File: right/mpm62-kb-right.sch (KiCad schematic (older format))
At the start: 86 parts

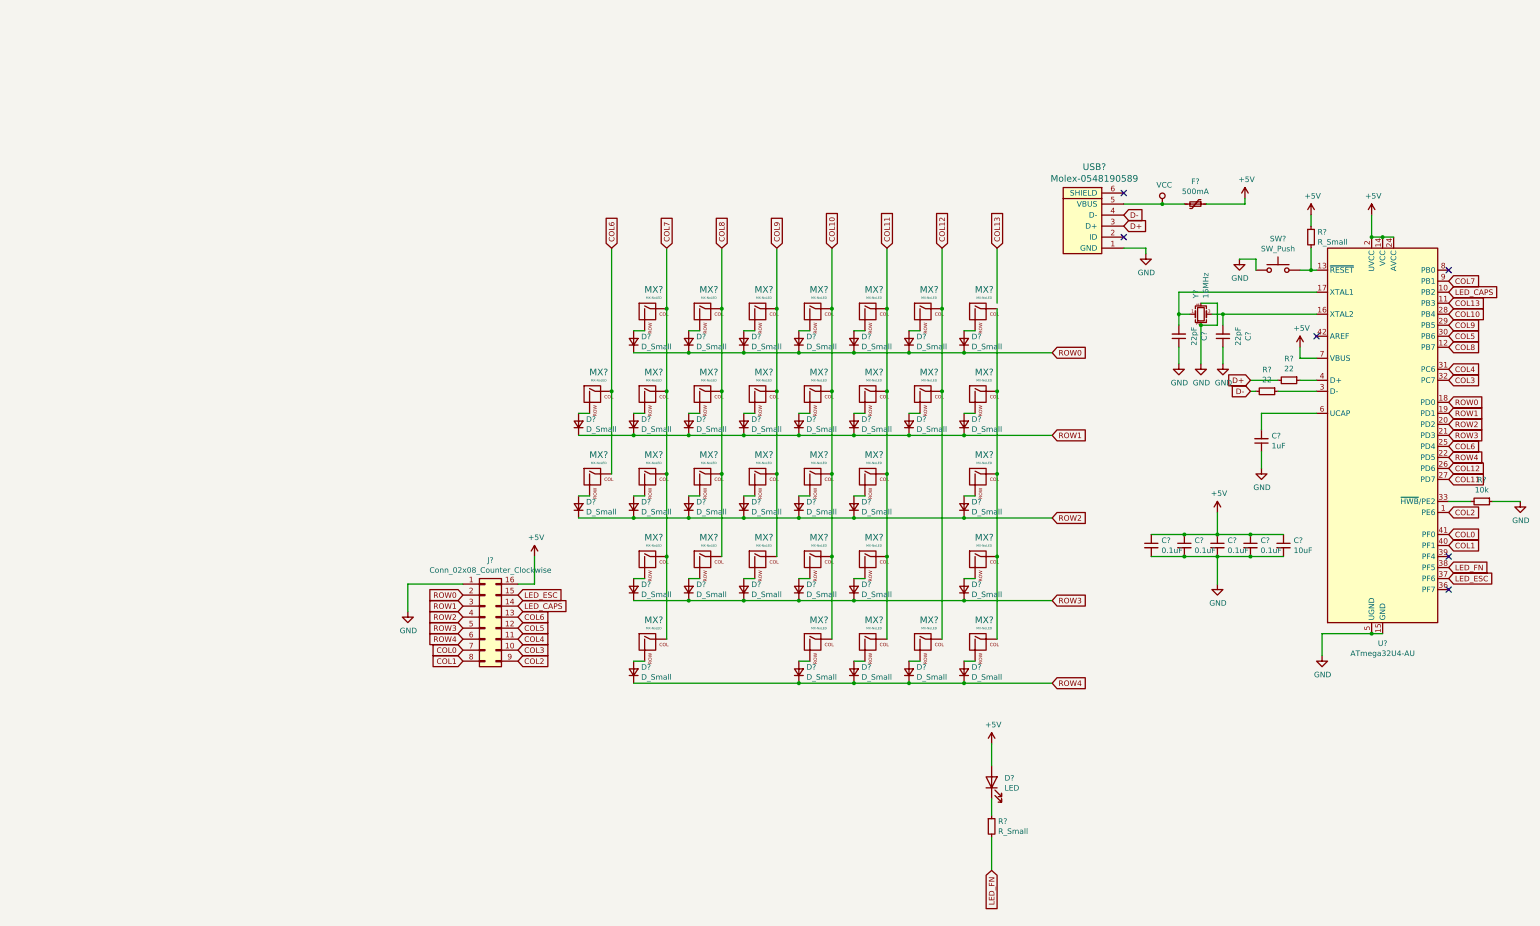
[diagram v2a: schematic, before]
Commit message: Annotated components
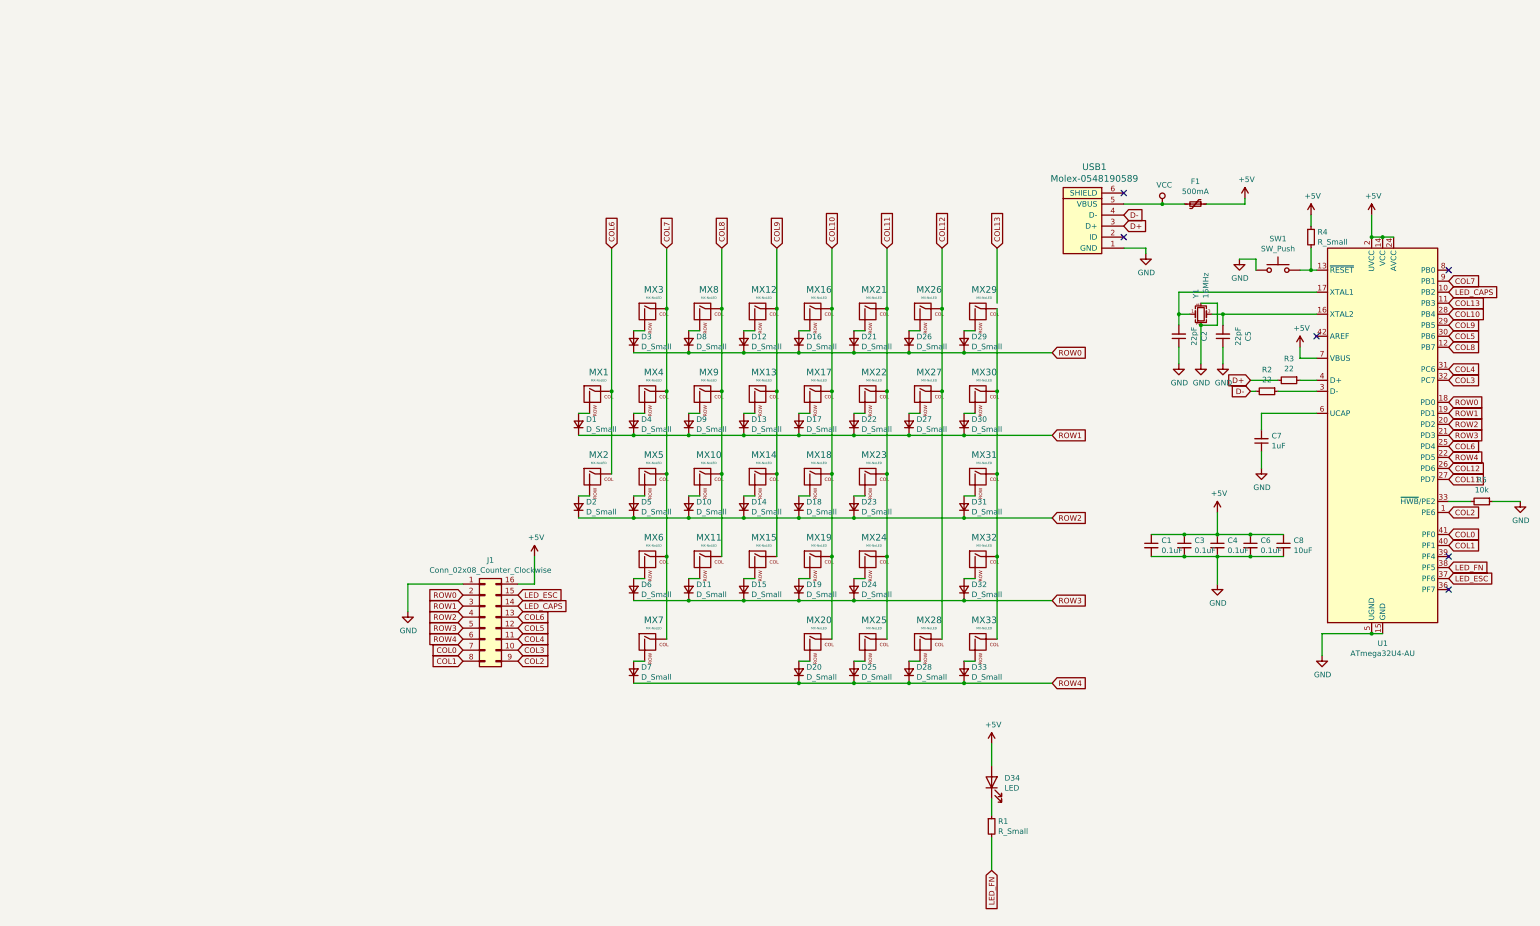
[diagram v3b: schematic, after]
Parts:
- gave numbers to parts that had none: 86

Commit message: Assigned footprints
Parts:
- C1, C2, C3, C4, C5, C6, C7, C8: footprint (none) -> Capacitor_SMD:C_0805_2012Metric
- D1, D10, D11, D12, D13, D14, D15, D16, D17, D18, D19, D2, D20, D21, D22, D23, D24, D25, D26, D27, D28, D29, D3, D30, D31, D32, D33, D4, D5, D6, D7, D8, D9: footprint (none) -> Diode_SMD:D_SOD-123
- D34: footprint (none) -> LED_SMD:LED_0805_2012Metric
- F1: footprint (none) -> Fuse:Fuse_1206_3216Metric
- J1: footprint (none) -> Connector_PinSocket_2.54mm:PinSocket_2x08_P2.54mm_Vertical
- MX1, MX10, MX11, MX12, MX13, MX14, MX15, MX16, MX17, MX18, MX19, MX2, MX21, MX22, MX23, MX24, MX26, MX27, MX3, MX4, MX5, MX6, MX8, MX9: footprint (none) -> MX_Alps_Hybrid:MX-1U-NoLED
- MX20, MX25, MX28, MX33: footprint (none) -> MX_Alps_Hybrid:MX-1.25U-NoLED
- MX29: footprint (none) -> MX_Alps_Hybrid:MX-2U-NoLED
- MX30: footprint (none) -> MX_Alps_Hybrid:MX-1.5U-NoLED
- MX31: footprint (none) -> MX_Alps_Hybrid:MX-2.25U-NoLED
- MX32: footprint (none) -> MX_Alps_Hybrid:MX-2.75U-NoLED
- MX7: footprint (none) -> MX_Alps_Hybrid:MX-3U-NoLED
- R1, R2, R3, R4, R5: footprint (none) -> Resistor_SMD:R_0805_2012Metric
- SW1: footprint (none) -> random-keyboard-parts:SKQG-1155865
- USB1: footprint (none) -> random-keyboard-parts:Molex-0548190589
- Y1: footprint (none) -> Crystal:Crystal_SMD_3225-4Pin_3.2x2.5mm

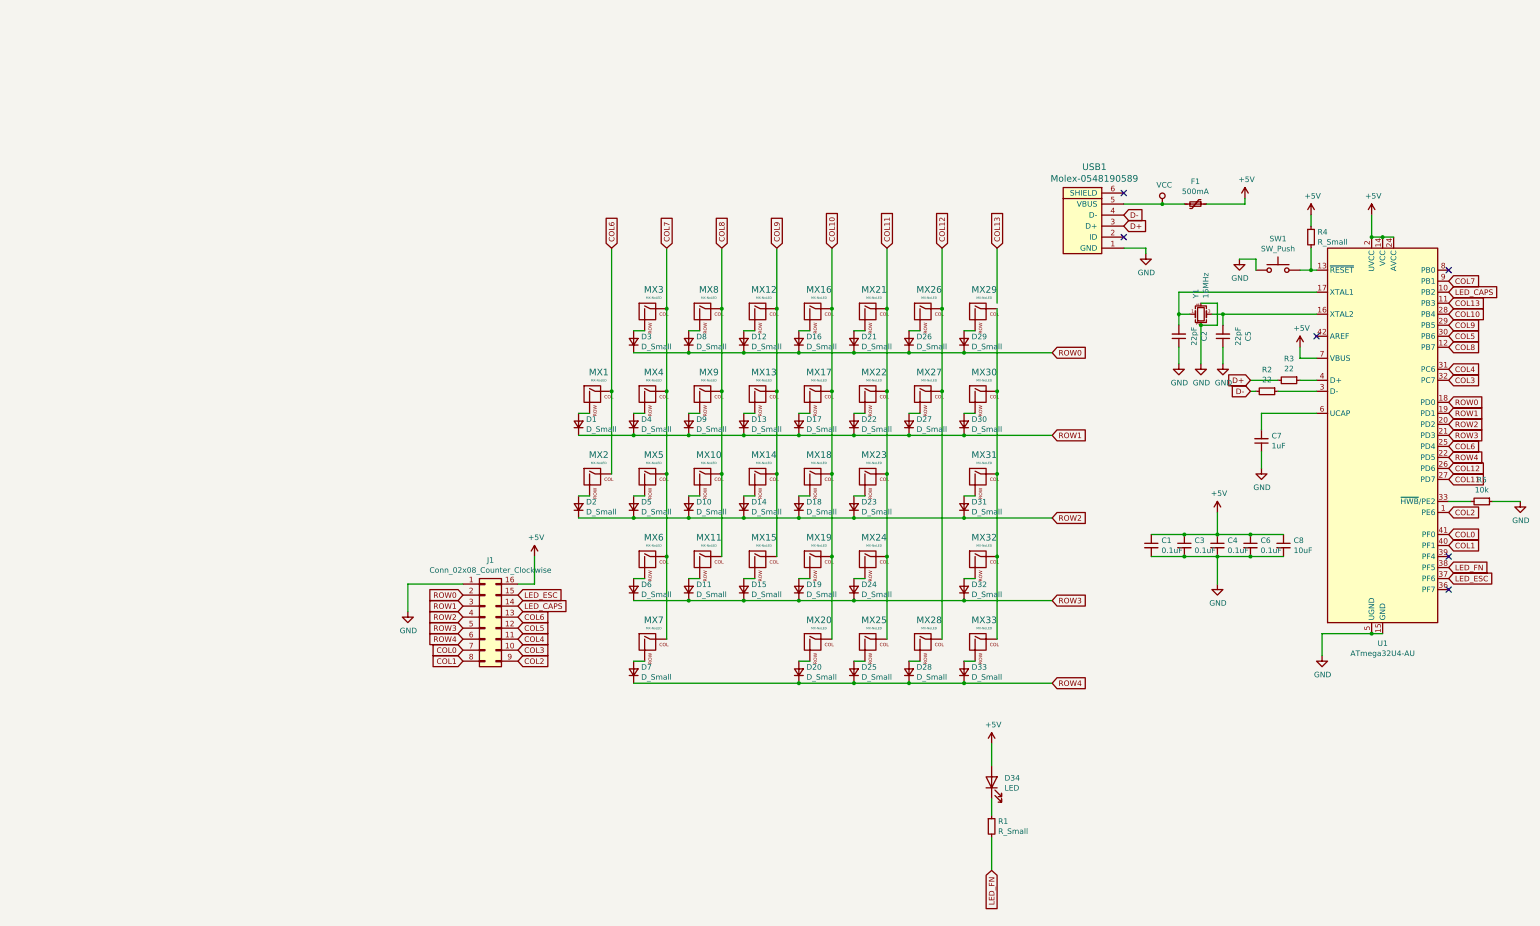
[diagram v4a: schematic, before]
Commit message: Schematic and pre-routed right-side based on mcp23018
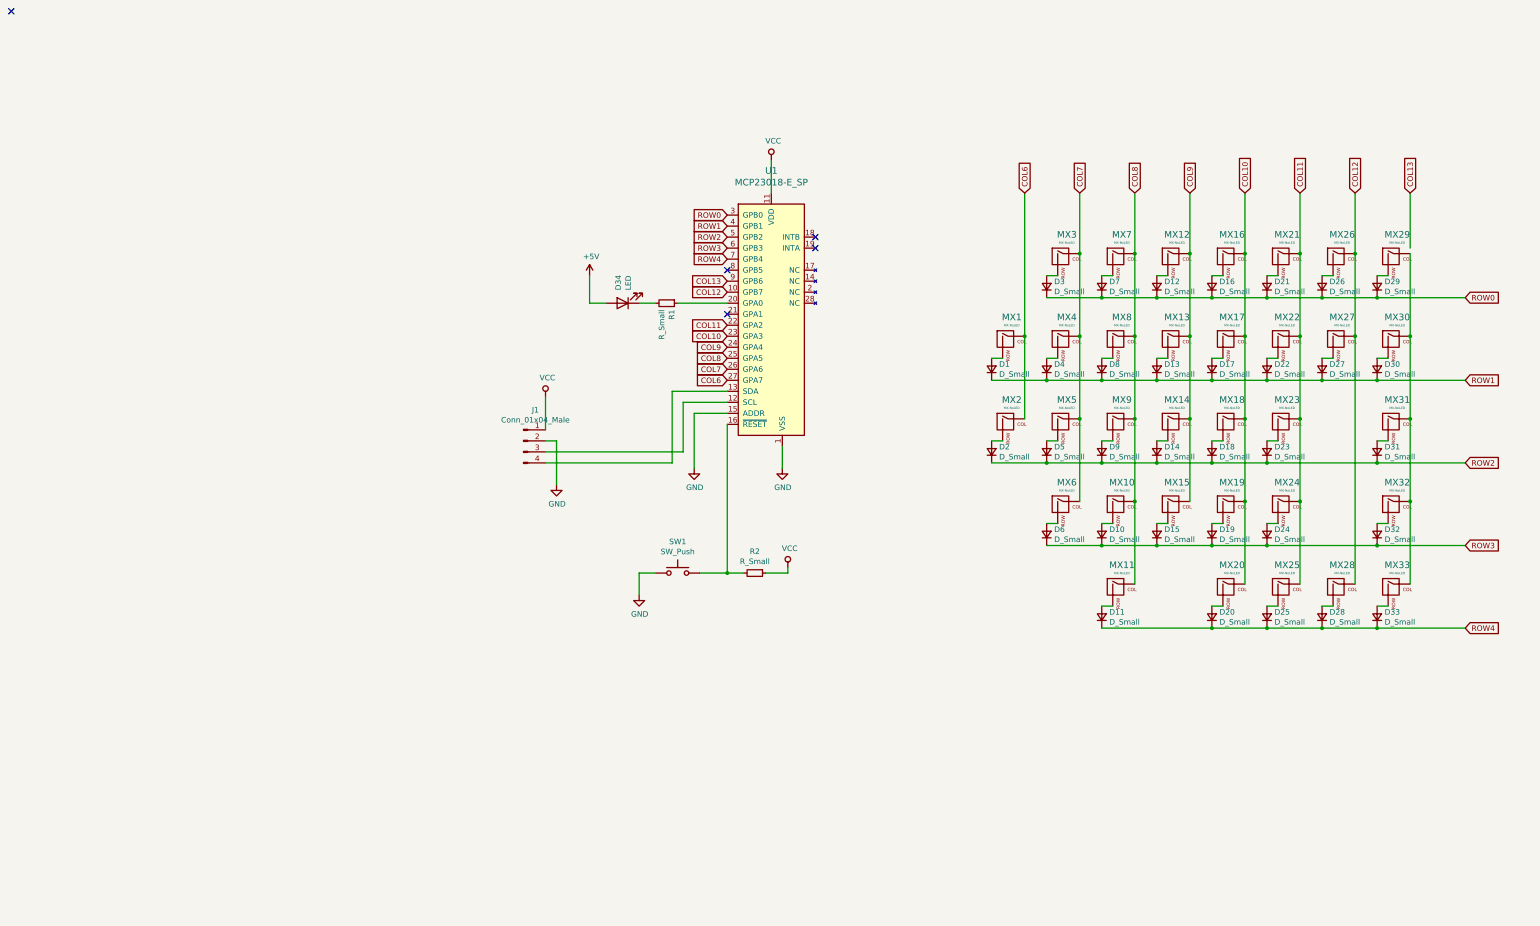
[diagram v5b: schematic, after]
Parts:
- removed C1, C3, C4, C6: 0.1uF, Capacitor_SMD:C_0805_2012Metric, symbol Device:C_Small
- removed C2, C5: 22pF, Capacitor_SMD:C_0805_2012Metric, symbol Device:C_Small
- removed C7: 1uF, Capacitor_SMD:C_0805_2012Metric, symbol Device:C_Small
- removed C8: 10uF, Capacitor_SMD:C_0805_2012Metric, symbol Device:C_Small
- removed F1: 500mA, Fuse:Fuse_1206_3216Metric, symbol Device:Polyfuse_Small
- removed J1: Conn_02x08_Counter_Clockwise, Connector_PinSocket_2.54mm:PinSocket_2x08_P2.54mm_Vertical, symbol Connector_Generic:Conn_02x08_Counter_Clockwise
- removed R3: 22, Resistor_SMD:R_0805_2012Metric, symbol Device:R_Small
- removed R4: R_Small, Resistor_SMD:R_0805_2012Metric, symbol Device:R_Small
- removed R5: 10k, Resistor_SMD:R_0805_2012Metric, symbol Device:R_Small
- removed U1: ATmega32U4-AU, Package_QFP:TQFP-44_10x10mm_P0.8mm, symbol MCU_Microchip_ATmega:ATmega32U4-AU
- removed USB1: Molex-0548190589, random-keyboard-parts:Molex-0548190589, symbol random-keyboard-parts:Molex-0548190589
- removed Y1: 16MHz, Crystal:Crystal_SMD_3225-4Pin_3.2x2.5mm, symbol Device:Crystal_GND24_Small
- added J1: Conn_01x04_Male, Connector_PinHeader_2.54mm:PinHeader_1x04_P2.54mm_Vertical, symbol Connector:Conn_01x04_Male
- added U1: MCP23018-E_SP, digikey-footprints:DIP-28_W7.62mm, symbol dk_Interface-I-O-Expanders:MCP23018-E_SP
- D1, D12, D13, D14, D15, D16, D17, D18, D19, D2, D20, D21, D22, D23, D24, D25, D26, D27, D28, D29, D3, D30, D31, D32, D33, D4, D5, D6: footprint Diode_SMD:D_SOD-123 -> Diode_THT:D_DO-35_SOD27_P7.62mm_Horizontal
- D10: renamed from D11; footprint Diode_SMD:D_SOD-123 -> Diode_THT:D_DO-35_SOD27_P7.62mm_Horizontal
- D11: renamed from D7; footprint Diode_SMD:D_SOD-123 -> Diode_THT:D_DO-35_SOD27_P7.62mm_Horizontal
- D34: footprint LED_SMD:LED_0805_2012Metric -> LED_THT:LED_D3.0mm
- D7: renamed from D8; footprint Diode_SMD:D_SOD-123 -> Diode_THT:D_DO-35_SOD27_P7.62mm_Horizontal
- D8: renamed from D9; footprint Diode_SMD:D_SOD-123 -> Diode_THT:D_DO-35_SOD27_P7.62mm_Horizontal
- D9: renamed from D10; footprint Diode_SMD:D_SOD-123 -> Diode_THT:D_DO-35_SOD27_P7.62mm_Horizontal
- R1: footprint Resistor_SMD:R_0805_2012Metric -> Resistor_THT:R_Axial_DIN0204_L3.6mm_D1.6mm_P5.08mm_Vertical
- R2: value 22 -> R_Small; footprint Resistor_SMD:R_0805_2012Metric -> Resistor_THT:R_Axial_DIN0204_L3.6mm_D1.6mm_P5.08mm_Vertical
- renumbered MX11 to MX10, MX7 to MX11, MX8 to MX7, MX9 to MX8, MX10 to MX9
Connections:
- net D- is gone; now on an unnamed net: R2.2
- net COL10: now also U1.23 (GPA3)
- net COL11: now also U1.22 (GPA2)
- net COL12: now also U1.10 (GPB7)
- net COL13: now also U1.9 (GPB6)
- net COL6: now also U1.27 (GPA7)
- net COL7: now also U1.26 (GPA6); no longer MX11.1 (COL)
- net COL8: now also MX11.1 (COL), U1.25 (GPA5)
- net COL9: now also U1.24 (GPA4)
- net GND: now also J1.2 (Pin_2), U1.1 (VSS), U1.15 (ADDR)
- net ROW0: now also U1.3 (GPB0)
- net ROW1: now also U1.4 (GPB1)
- net ROW2: now also U1.5 (GPB2)
- net ROW3: now also U1.6 (GPB3)
- net ROW4: now also U1.7 (GPB4)
- net VCC: now also R2.1, J1.1 (Pin_1), U1.11 (VDD)
- net at SW1.2: now also U1.16 (~RESET)
- net at R1.1: now also U1.20 (GPA0); no longer D34.1 (K)
- net LED_FN: no longer names the net of R1.2
- net LED_FN: now also D34.1 (K)
- new net: J1.3 (Pin_3), U1.12 (SCL)
- new net: J1.4 (Pin_4), U1.13 (SDA)
- no-connect marks 6 -> 5
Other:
- moved on the sheet: D1, D10, D11, D12, D13, D14, D15, D16, D17, D18, D19, D2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

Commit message: Fix resistor footprint, clean up layout.
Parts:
- R1, R2: footprint Resistor_THT:R_Axial_DIN0204_L3.6mm_D1.6mm_P5.08mm_Vertical -> Resistor_THT:R_Axial_DIN0204_L3.6mm_D1.6mm_P5.08mm_Horizontal
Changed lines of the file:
@@
 F 0 "R1" H 3309 2046 50  0000 L CNN
 F 1 "R_Small" H 3309 1955 50  0000 L CNN
-F 2 "Resistor_THT:R_Axial_DIN0204_L3.6mm_D1.6mm_P5.08mm_Vertical" H 3250 2000 50  0001 C CNN
+F 2 "Resistor_THT:R_Axial_DIN0204_L3.6mm_D1.6mm_P5.08mm_Horizontal" H 3250 2000 50  0001 C CNN
 F 3 "~" H 3250 2000 50  0001 C CNN
 	1    3250 2000
@@
 F 0 "R2" V 3854 4450 50  0000 C CNN
 F 1 "R_Small" V 3945 4450 50  0000 C CNN
-F 2 "Resistor_THT:R_Axial_DIN0204_L3.6mm_D1.6mm_P5.08mm_Vertical" H 4050 4450 50  0001 C CNN
+F 2 "Resistor_THT:R_Axial_DIN0204_L3.6mm_D1.6mm_P5.08mm_Horizontal" H 4050 4450 50  0001 C CNN
 F 3 "~" H 4050 4450 50  0001 C CNN
 	1    4050 4450

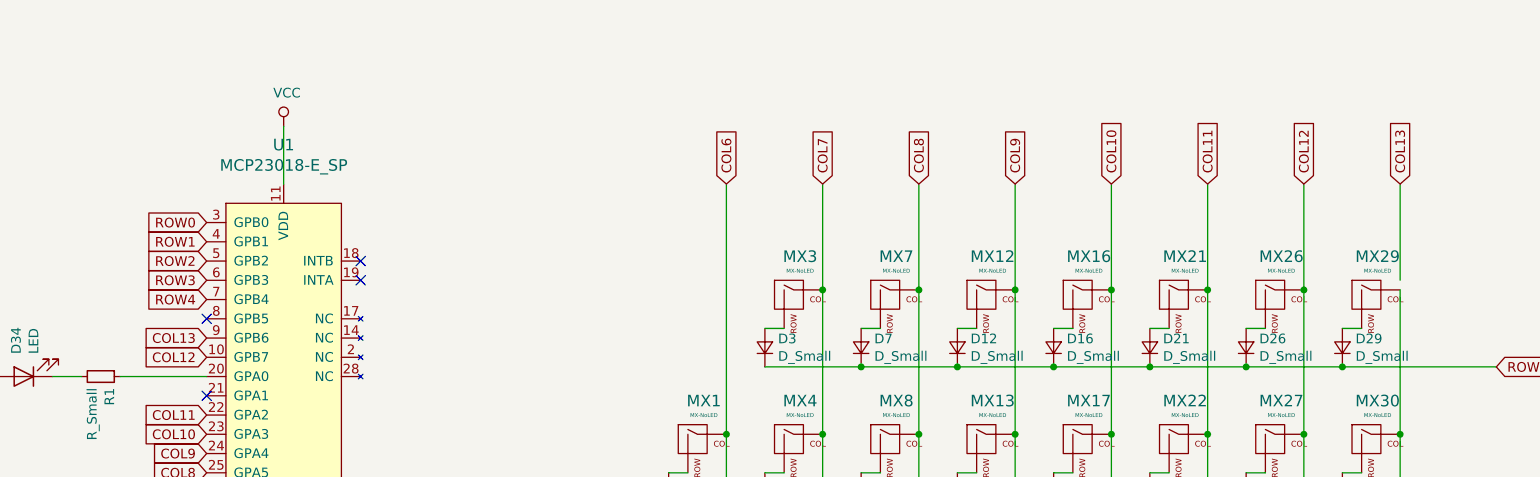
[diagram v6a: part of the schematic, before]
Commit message: Finished right side routing, some simplification, ground fill.
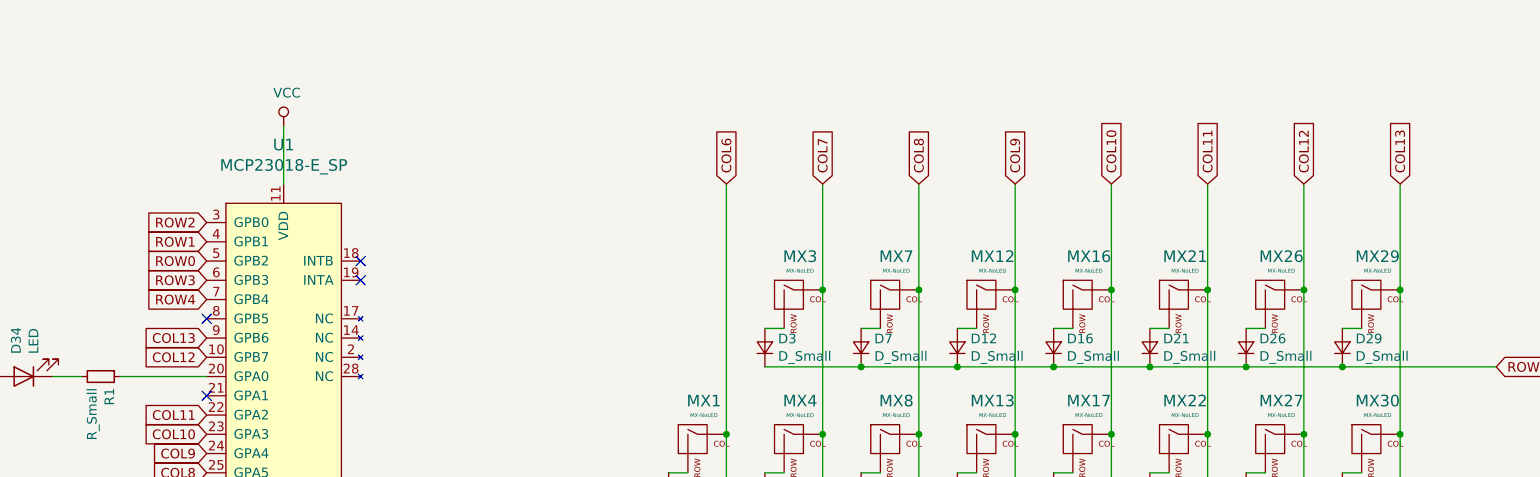
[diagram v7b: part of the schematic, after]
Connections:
- net COL13: now also MX29.1 (COL), MX30.1 (COL), MX31.1 (COL), MX32.1 (COL), MX33.1 (COL)
- net ROW0: now also U1.5 (GPB2); no longer U1.3 (GPB0)
- net ROW2: now also U1.3 (GPB0); no longer U1.5 (GPB2)
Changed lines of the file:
@@
 Connection ~ 9500 1550
-Wire Wire Line
-	10000 1500 10000 1000
 Wire Wire Line
 	8000 1550 8000 1000
@@
 Text GLabel 3800 2500 0    50   Input ~ 0
 COL8
-Text GLabel 3800 1200 0    50   Input ~ 0
+Text GLabel 3800 1400 0    50   Input ~ 0
 ROW0
 Text GLabel 3800 1300 0    50   Input ~ 0
 ROW1
-Text GLabel 3800 1400 0    50   Input ~ 0
+Text GLabel 3800 1200 0    50   Input ~ 0
 ROW2
 Text GLabel 3800 1500 0    50   Input ~ 0
@@
 	7200 4950 8200 4950
 Connection ~ 8200 4950
+Wire Wire Line
+	10000 1000 10000 1550
+Connection ~ 10000 1550
 $EndSCHEMATC
